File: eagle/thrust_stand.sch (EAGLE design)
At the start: 37 parts, among them IC1 7805TV, Q1 16Mhz, Q2 IRF510, Q3 IRF510, Q4 IRF510, U2 ATMEGA328P_PDIP

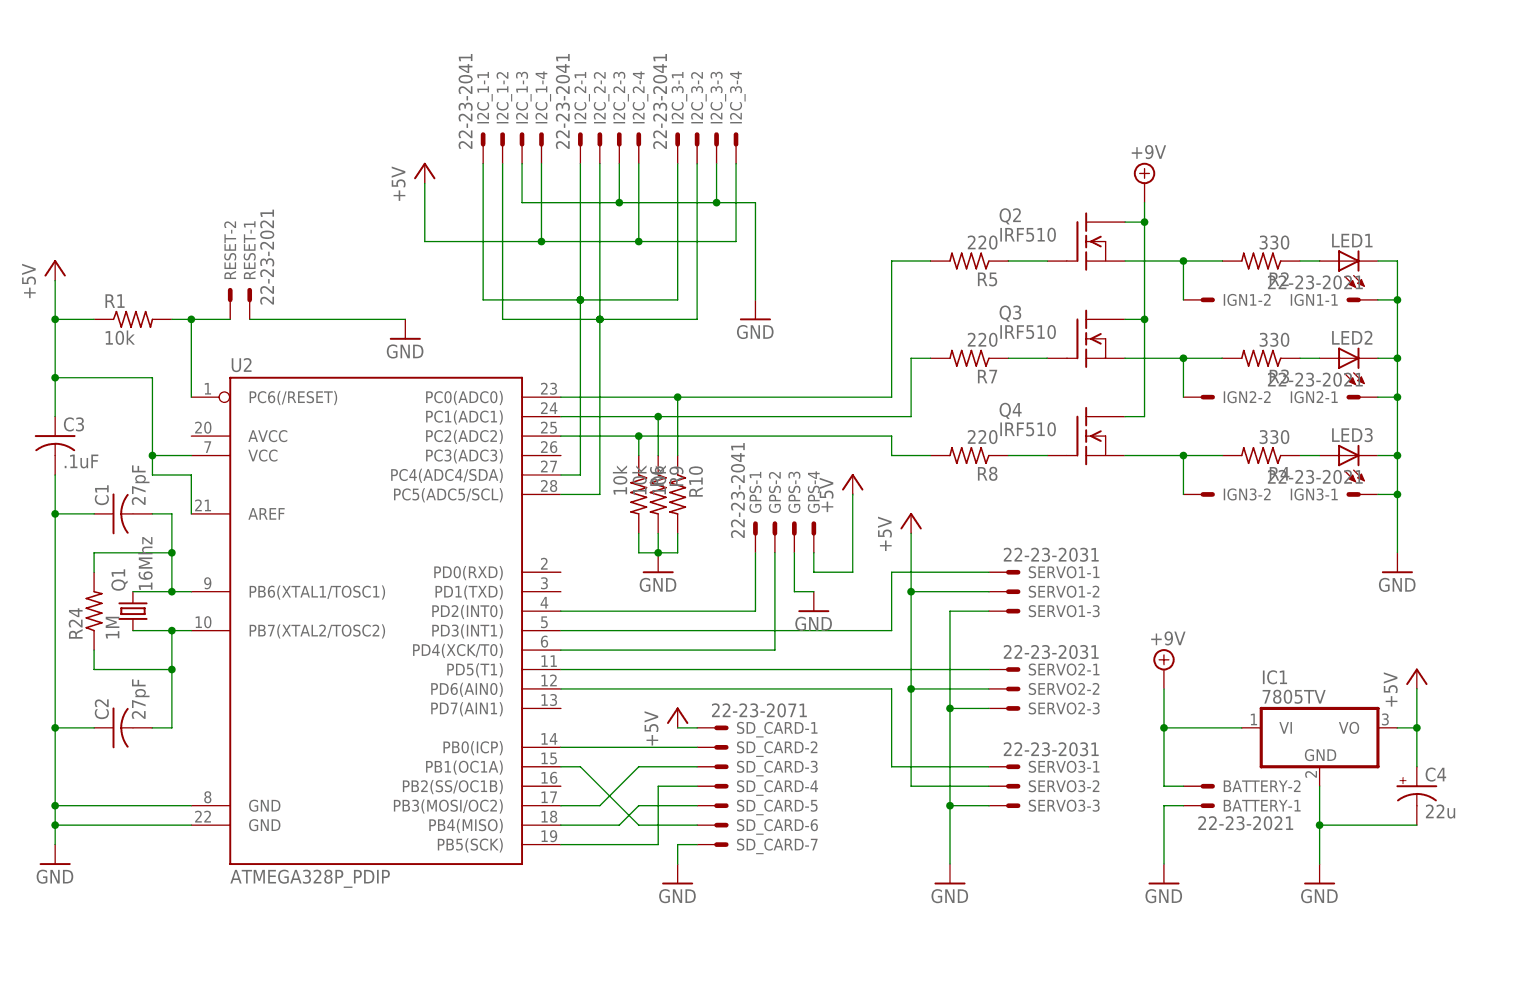
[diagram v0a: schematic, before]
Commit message: added hx711 to schemo
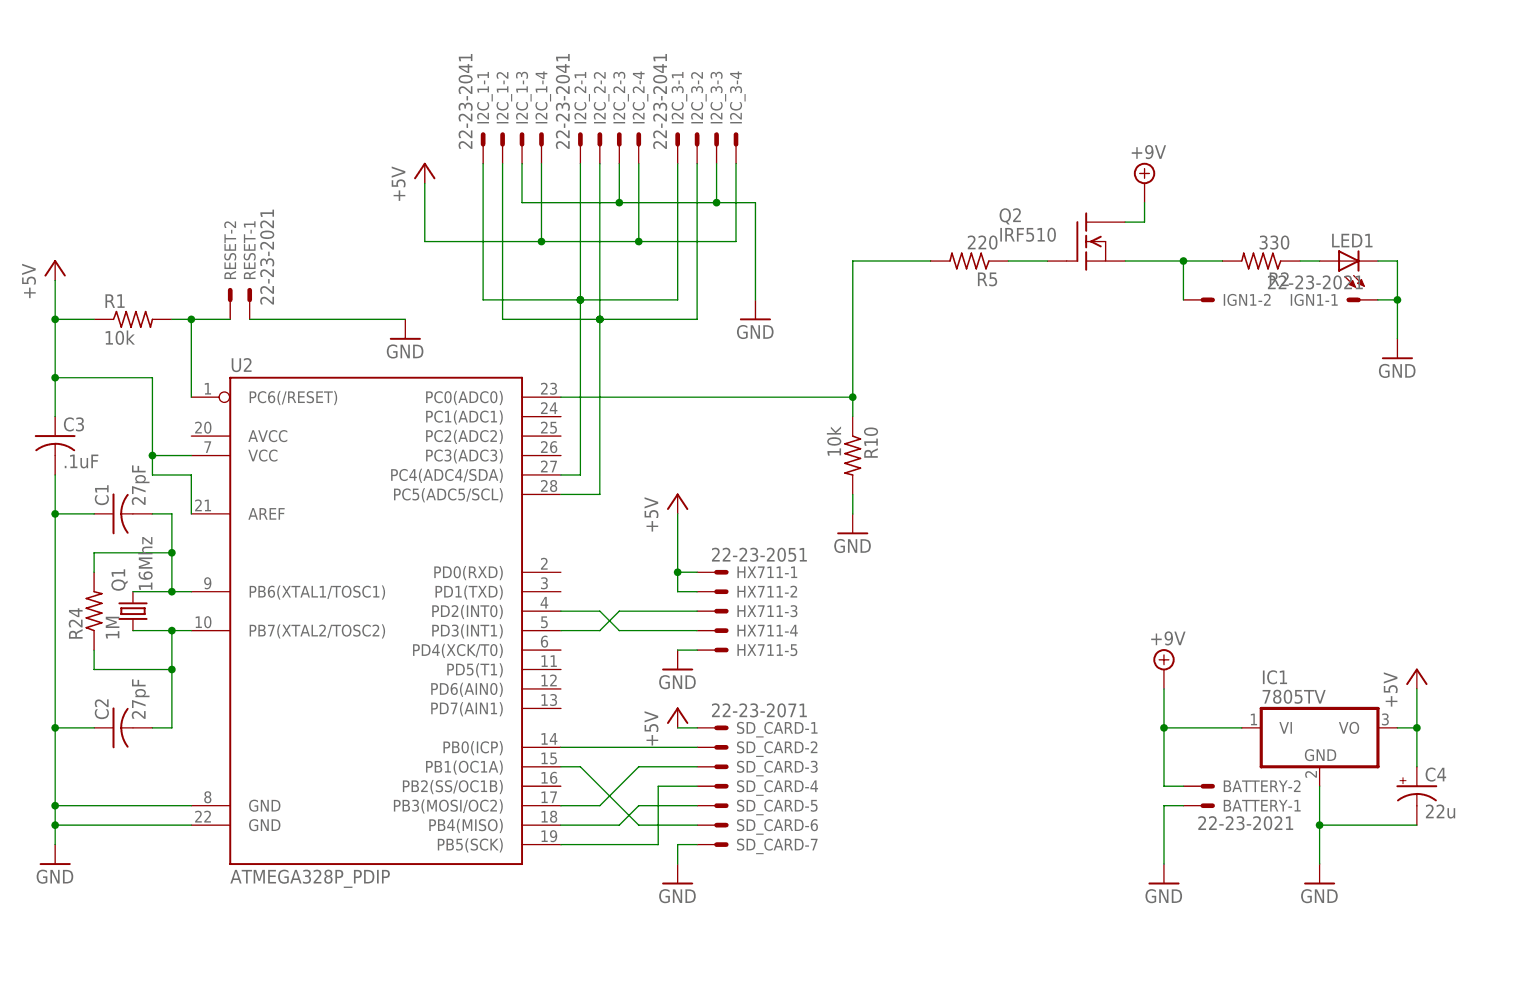
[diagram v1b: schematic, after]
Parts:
- removed GPS: 22-23-2041, con-molex:22-23-2041
- removed IGN2, IGN3: 22-23-2021, con-molex:22-23-2021
- removed LED2, LED3: (no value), led:LED5MM
- removed Q3, Q4: IRF510, transistor-fet:IRF510
- removed R3, R4: 330, rcl:R-US_0207/7
- removed R6, R9: 10k, rcl:R-US_0207/2V
- removed R7, R8: 220, rcl:R-US_0207/7
- removed SERVO1, SERVO2, SERVO3: 22-23-2031, con-molex:22-23-2031
- added HX711: 22-23-2051, con-molex:22-23-2051
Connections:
- removed net N$13: Q3.G, R7.1
- removed net N$14: Q4.G, R8.1
- removed net N$15: SERVO1-1.S, U2.PD3(INT1)
- removed net N$16: SERVO2-1.S, U2.PD5(T1)
- removed net N$17: SERVO3-1.S, U2.PD6(AIN0)
- removed net N$19: R7.2, R9.1, U2.PC1(ADC1)
- removed net N$20: R6.1, R8.2, U2.PC2(ADC2)
- removed net N$22: LED2.A, R3.1
- removed net N$23: LED3.A, R4.1
- removed net N$25: IGN2-2.S, Q3.S, R3.2
- removed net N$26: IGN3-2.S, Q4.S, R4.2
- net +5V: now also HX711-1.S, HX711-2.S; no longer GPS-4.S, SERVO1-2.S, SERVO2-2.S, SERVO3-2.S
- net +9V: no longer Q3.D, Q4.D
- net GND: now also HX711-5.S; no longer GPS-3.S, IGN2-1.S, IGN3-1.S, LED2.C, LED3.C, R6.2, R9.2, SERVO1-3.S, SERVO2-3.S, SERVO3-3.S
- net N$3: now also HX711-3.S, U2.PD3(INT1); no longer GPS-1.S, U2.PD2(INT0)
- net N$6: now also HX711-4.S, U2.PD2(INT0); no longer GPS-2.S, U2.PD4(XCK/T0)
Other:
- moved on the sheet: R10

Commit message: added speaker to schemo
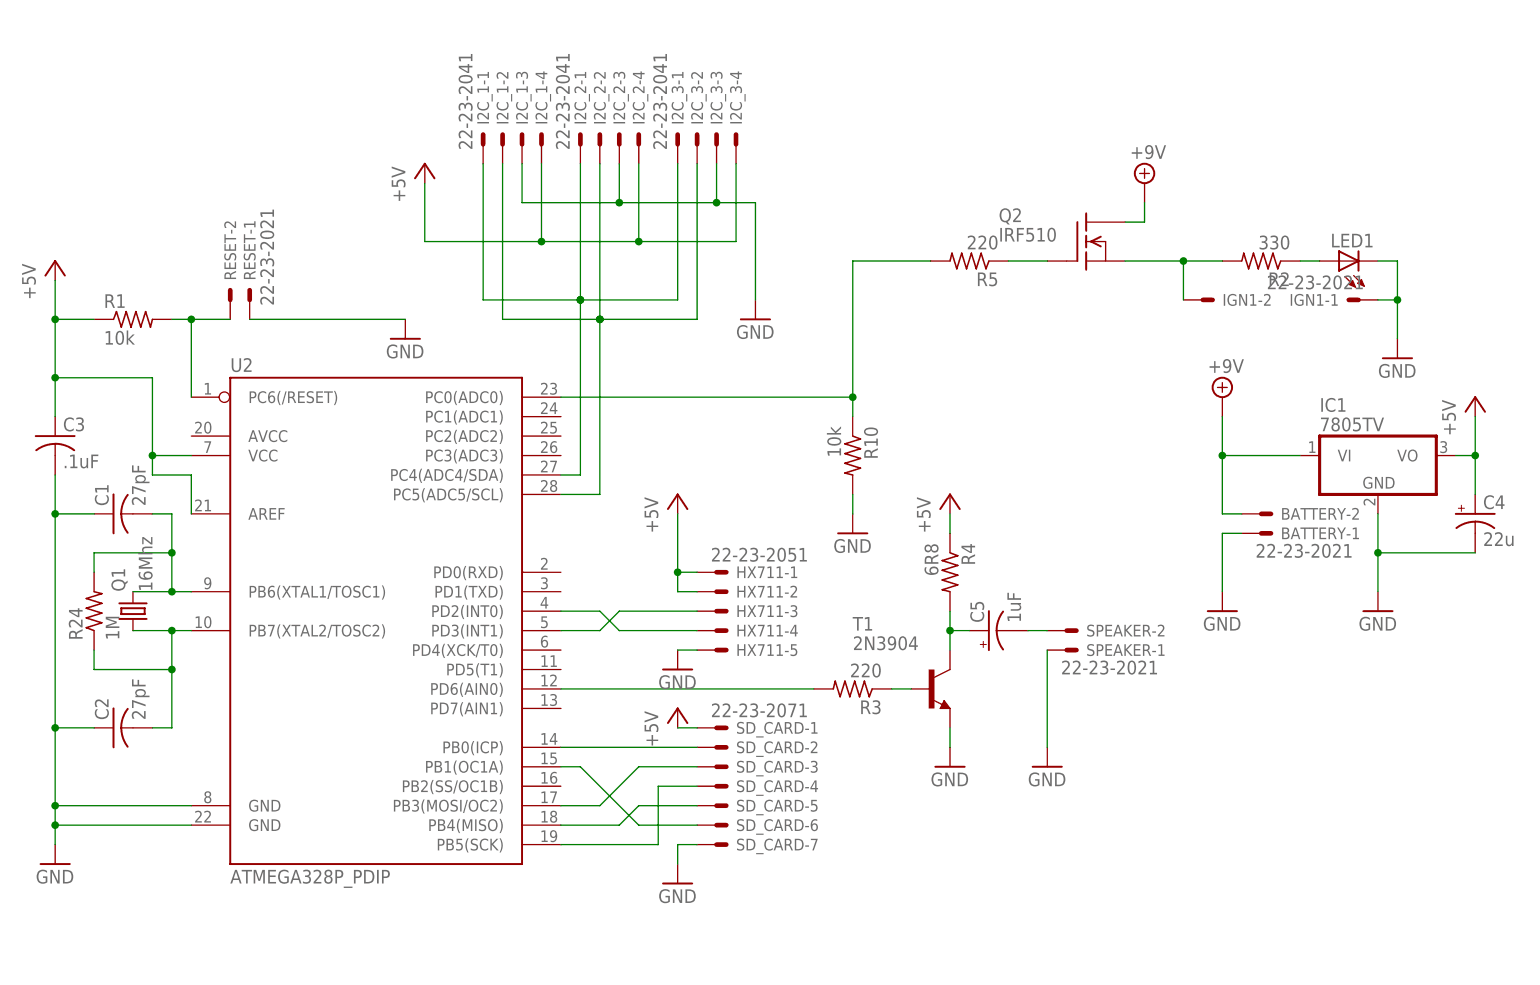
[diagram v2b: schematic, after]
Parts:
- added C5: 1uF, rcl:CPOL-USB45181A
- added R3: 220, rcl:R-US_0207/7
- added R4: 6R8, rcl:R-US_0207/7
- added SPEAKER: 22-23-2021, con-molex:22-23-2021
- added T1: 2N3904, transistor:2N3904
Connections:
- new net N$13: R3.2, U2.PD6(AIN0)
- new net N$14: R3.1, T1.B
- new net N$15: C5.+, R4.2, T1.C
- new net N$16: C5.-, SPEAKER-2.S
- net +5V: now also R4.1
- net GND: now also SPEAKER-1.S, T1.E
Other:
- moved on the sheet: BATTERY-1, BATTERY-2, C4, IC1
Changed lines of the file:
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@@
 <part name="P+4" library="supply1" deviceset="+5V" device=""/>
 <part name="GND4" library="supply1" deviceset="GND" device=""/>
+<part name="T1" library="transistor" deviceset="2N3904" device=""/>
+<part name="R3" library="rcl" deviceset="R-US_" device="0207/7" value="220"/>
+<part name="C5" library="rcl" deviceset="CPOL-US" device="B45181A" value="1uF"/>
+<part name="SPEAKER" library="con-molex" deviceset="22-23-2021" device=""/>
+<part name="R4" library="rcl" deviceset="R-US_" device="0207/7" value="6R8"/>
+<part name="P+5" library="supply1" deviceset="+5V" device=""/>
+<part name="GND7" library="supply1" deviceset="GND" device=""/>
+<part name="GND10" library="supply1" deviceset="GND" device=""/>
 </parts>
 <sheets>
@@
 <instance part="LED1" gate="G$1" x="142.24" y="91.44" rot="R90"/>
 <instance part="GND6" gate="1" x="149.86" y="78.74"/>
-<instance part="IC1" gate="A1" x="139.7" y="30.48"/>
-<instance part="SUPPLY2" gate="G$1" x="119.38" y="38.1"/>
-<instance part="C4" gate="G$1" x="152.4" y="22.86"/>
-<instance part="P+6" gate="1" x="152.4" y="38.1"/>
-<instance part="GND8" gate="1" x="139.7" y="10.16"/>
-<instance part="BATTERY" gate="-1" x="124.46" y="20.32" rot="MR180"/>
-<instance part="BATTERY" gate="-2" x="124.46" y="22.86" rot="MR180"/>
-<instance part="GND9" gate="1" x="119.38" y="10.16"/>
+<instance part="IC1" gate="A1" x="147.32" y="66.04"/>
+<instance part="SUPPLY2" gate="G$1" x="127" y="73.66"/>
+<instance part="C4" gate="G$1" x="160.02" y="58.42"/>
+<instance part="P+6" gate="1" x="160.02" y="73.66"/>
+<instance part="GND8" gate="1" x="147.32" y="45.72"/>
+<instance part="BATTERY" gate="-1" x="132.08" y="55.88" rot="MR180"/>
+<instance part="BATTERY" gate="-2" x="132.08" y="58.42" rot="MR180"/>
+<instance part="GND9" gate="1" x="127" y="45.72"/>
 <instance part="R5" gate="G$1" x="93.98" y="91.44" rot="R180"/>
 <instance part="R10" gate="G$1" x="78.74" y="66.04" rot="R270"/>
@@
 <instance part="P+4" gate="1" x="55.88" y="60.96"/>
 <instance part="GND4" gate="1" x="55.88" y="38.1"/>
+<instance part="T1" gate="G1" x="88.9" y="35.56"/>
+<instance part="R3" gate="G$1" x="78.74" y="35.56" rot="R180"/>
+<instance part="C5" gate="G$1" x="96.52" y="43.18" rot="R90"/>
+<instance part="SPEAKER" gate="-1" x="106.68" y="40.64" rot="MR180"/>
+<instance part="SPEAKER" gate="-2" x="106.68" y="43.18" rot="MR180"/>
+<instance part="R4" gate="G$1" x="91.44" y="50.8" rot="R270"/>
+<instance part="P+5" gate="1" x="91.44" y="60.96"/>
+<instance part="GND7" gate="1" x="91.44" y="25.4"/>
+<instance part="GND10" gate="1" x="104.14" y="25.4"/>
 </instances>
 <busses>
@@
 <pinref part="IC1" gate="A1" pin="VO"/>
 <pinref part="P+6" gate="1" pin="+5V"/>
-<wire x1="149.86" y1="30.48" x2="152.4" y2="30.48" width="0.1524" layer="91"/>
-<wire x1="152.4" y1="30.48" x2="152.4" y2="35.56" width="0.1524" layer="91"/>
+<wire x1="157.48" y1="66.04" x2="160.02" y2="66.04" width="0.1524" layer="91"/>
+<wire x1="160.02" y1="66.04" x2="160.02" y2="71.12" width="0.1524" layer="91"/>
 <pinref part="C4" gate="G$1" pin="+"/>
-<wire x1="152.4" y1="25.4" x2="152.4" y2="30.48" width="0.1524" layer="91"/>
-<junction x="152.4" y="30.48"/>
+<wire x1="160.02" y1="60.96" x2="160.02" y2="66.04" width="0.1524" layer="91"/>
+<junction x="160.02" y="66.04"/>
 </segment>
 <segment>
@@
 <wire x1="55.88" y1="48.26" x2="55.88" y2="50.8" width="0.1524" layer="91"/>
 <junction x="55.88" y="50.8"/>
+</segment>
+<segment>
+<pinref part="R4" gate="G$1" pin="1"/>
+<pinref part="P+5" gate="1" pin="+5V"/>
+<wire x1="91.44" y1="55.88" x2="91.44" y2="58.42" width="0.1524" layer="91"/>
 </segment>
 </net>
@@
 <pinref part="IC1" gate="A1" pin="GND"/>
 <pinref part="GND8" gate="1" pin="GND"/>
-<wire x1="139.7" y1="22.86" x2="139.7" y2="17.78" width="0.1524" layer="91"/>
+<wire x1="147.32" y1="58.42" x2="147.32" y2="53.34" width="0.1524" layer="91"/>
 <pinref part="C4" gate="G$1" pin="-"/>
-<wire x1="139.7" y1="17.78" x2="139.7" y2="12.7" width="0.1524" layer="91"/>
-<wire x1="152.4" y1="17.78" x2="139.7" y2="17.78" width="0.1524" layer="91"/>
-<junction x="139.7" y="17.78"/>
+<wire x1="147.32" y1="53.34" x2="147.32" y2="48.26" width="0.1524" layer="91"/>
+<wire x1="160.02" y1="53.34" x2="147.32" y2="53.34" width="0.1524" layer="91"/>
+<junction x="147.32" y="53.34"/>
 </segment>
 <segment>
 <pinref part="BATTERY" gate="-1" pin="S"/>
 <pinref part="GND9" gate="1" pin="GND"/>
-<wire x1="121.92" y1="20.32" x2="119.38" y2="20.32" width="0.1524" layer="91"/>
-<wire x1="119.38" y1="20.32" x2="119.38" y2="12.7" width="0.1524" layer="91"/>
+<wire x1="129.54" y1="55.88" x2="127" y2="55.88" width="0.1524" layer="91"/>
+<wire x1="127" y1="55.88" x2="127" y2="48.26" width="0.1524" layer="91"/>
 </segment>
 <segment>
@@
 <pinref part="GND4" gate="1" pin="GND"/>
 <wire x1="58.42" y1="40.64" x2="55.88" y2="40.64" width="0.1524" layer="91"/>
+</segment>
+<segment>
+<pinref part="SPEAKER" gate="-1" pin="S"/>
+<pinref part="GND10" gate="1" pin="GND"/>
+<wire x1="104.14" y1="40.64" x2="104.14" y2="27.94" width="0.1524" layer="91"/>
+</segment>
+<segment>
+<pinref part="T1" gate="G1" pin="E"/>
+<pinref part="GND7" gate="1" pin="GND"/>
+<wire x1="91.44" y1="30.48" x2="91.44" y2="27.94" width="0.1524" layer="91"/>
 </segment>
 </net>
@@
 <pinref part="IC1" gate="A1" pin="VI"/>
 <pinref part="SUPPLY2" gate="G$1" pin="+9V"/>
-<wire x1="129.54" y1="30.48" x2="119.38" y2="30.48" width="0.1524" layer="91"/>
-<wire x1="119.38" y1="30.48" x2="119.38" y2="35.56" width="0.1524" layer="91"/>
+<wire x1="137.16" y1="66.04" x2="127" y2="66.04" width="0.1524" layer="91"/>
+<wire x1="127" y1="66.04" x2="127" y2="71.12" width="0.1524" layer="91"/>
 <pinref part="BATTERY" gate="-2" pin="S"/>
-<wire x1="121.92" y1="22.86" x2="119.38" y2="22.86" width="0.1524" layer="91"/>
-<wire x1="119.38" y1="22.86" x2="119.38" y2="30.48" width="0.1524" layer="91"/>
-<junction x="119.38" y="30.48"/>
+<wire x1="129.54" y1="58.42" x2="127" y2="58.42" width="0.1524" layer="91"/>
+<wire x1="127" y1="58.42" x2="127" y2="66.04" width="0.1524" layer="91"/>
+<junction x="127" y="66.04"/>
 </segment>
 </net>
@@
 </segment>
 </net>
+<net name="N$13" class="0">
+<segment>
+<pinref part="R3" gate="G$1" pin="2"/>
+<pinref part="U2" gate="G$1" pin="PD6(AIN0)"/>
+<wire x1="73.66" y1="35.56" x2="40.64" y2="35.56" width="0.1524" layer="91"/>
+</segment>
+</net>
+<net name="N$14" class="0">
+<segment>
+<pinref part="R3" gate="G$1" pin="1"/>
+<pinref part="T1" gate="G1" pin="B"/>
+<wire x1="83.82" y1="35.56" x2="86.36" y2="35.56" width="0.1524" layer="91"/>
+</segment>
+</net>
+<net name="N$15" class="0">
+<segment>
+<pinref part="T1" gate="G1" pin="C"/>
+<pinref part="R4" gate="G$1" pin="2"/>
+<wire x1="91.44" y1="40.64" x2="91.44" y2="43.18" width="0.1524" layer="91"/>
+<pinref part="C5" gate="G$1" pin="+"/>
+<wire x1="91.44" y1="43.18" x2="91.44" y2="45.72" width="0.1524" layer="91"/>
+<wire x1="93.98" y1="43.18" x2="91.44" y2="43.18" width="0.1524" layer="91"/>
+<junction x="91.44" y="43.18"/>
+</segment>
+</net>
+<net name="N$16" class="0">
+<segment>
+<pinref part="SPEAKER" gate="-2" pin="S"/>
+<pinref part="C5" gate="G$1" pin="-"/>
+<wire x1="104.14" y1="43.18" x2="101.6" y2="43.18" width="0.1524" layer="91"/>
+</segment>
+</net>
